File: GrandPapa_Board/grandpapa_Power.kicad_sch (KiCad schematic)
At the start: 34 parts, among them U2 TPS61023DRLT, U5 FPF2124, U6 INA180

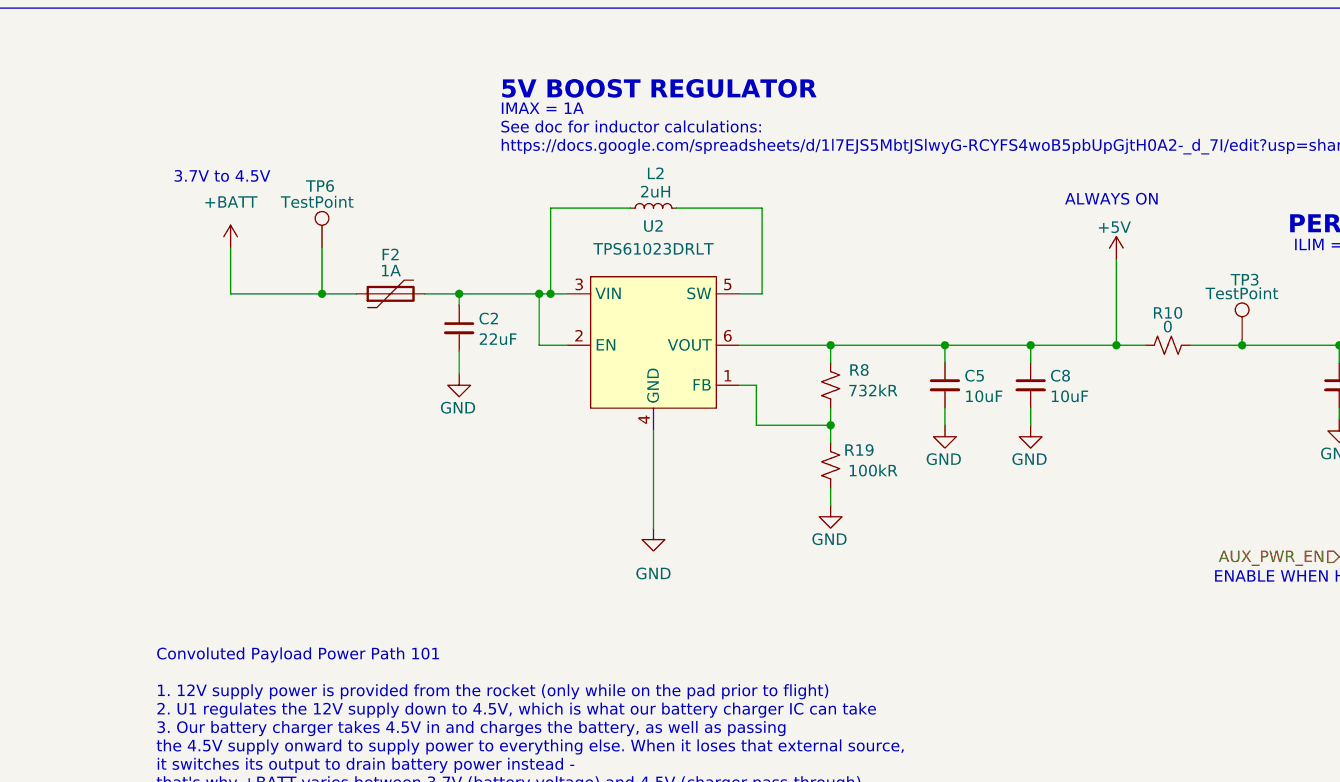
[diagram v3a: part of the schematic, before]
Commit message: Addded 5V boost and kalman board connector
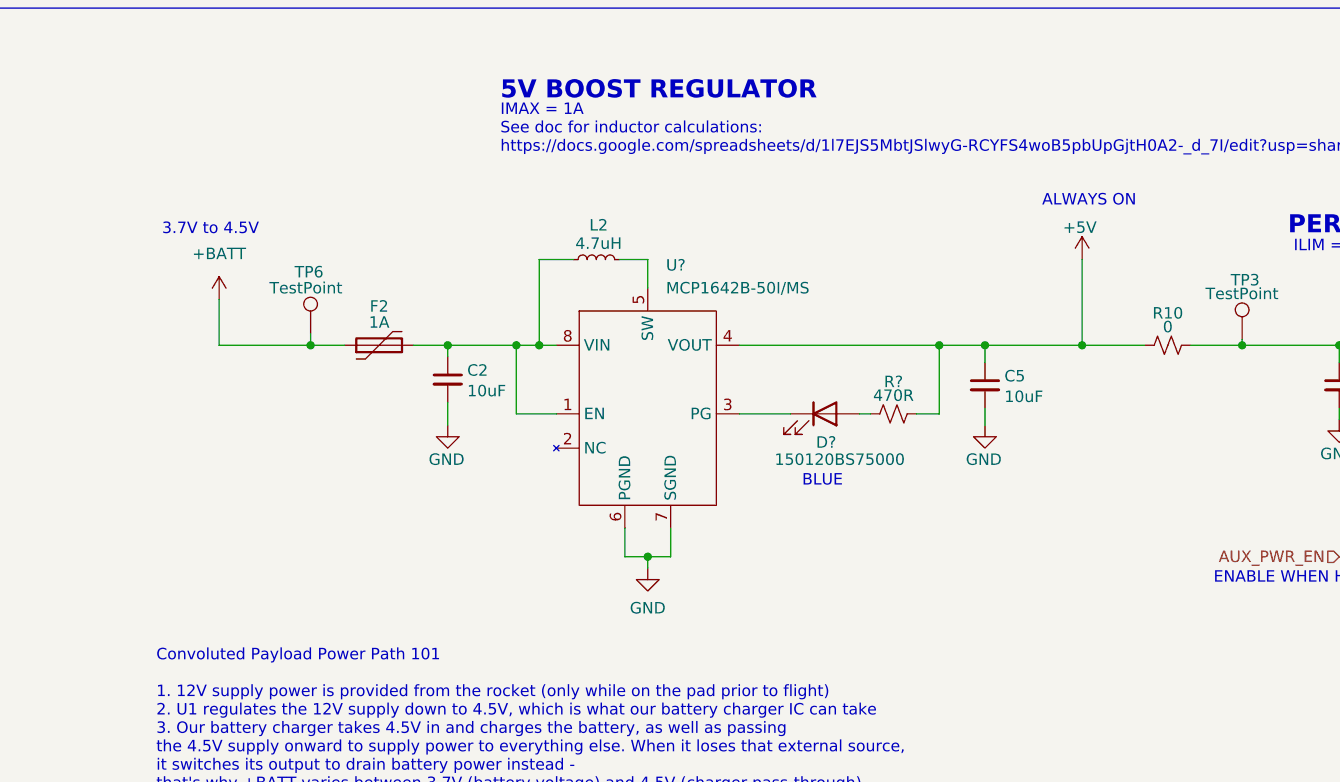
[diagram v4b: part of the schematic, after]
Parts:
- removed C8: 10uF, symbol Device:C_Small
- removed R19: 100kR, symbol Device:R_Small_US
- removed R8: 732kR, symbol Device:R_Small_US
- removed U2: TPS61023DRLT, symbol grandpapa board:TPS61023DRLT
- added D?: 150120BS75000, LED_SMD:LED_1206_3216Metric_Pad1.42x1.75mm_HandSolder, symbol Device:LED
- added R?: 470R, symbol Device:R_Small_US
- added U?: MCP1642B-50I/MS, symbol grandpapa board:MCP1642B/D-xx
- C2: value 22uF -> 10uF
- L2: value 2uH -> 4.7uH
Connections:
- net +5V: now also R?.2, U?.4 (VOUT)
- net GND: now also U?.6 (PGND), U?.7 (SGND)
- net at C2.1, F2.2, L2.1: now also U?.1 (EN), U?.8 (VIN)
- net at L2.2: now also U?.5 (SW)
- new net: D?.1 (K), U?.3 (PG)
- new net: D?.2 (A), R?.1
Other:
- note added: "BLUE"
- moved on the sheet: C2, C5, F2, L2, TP6

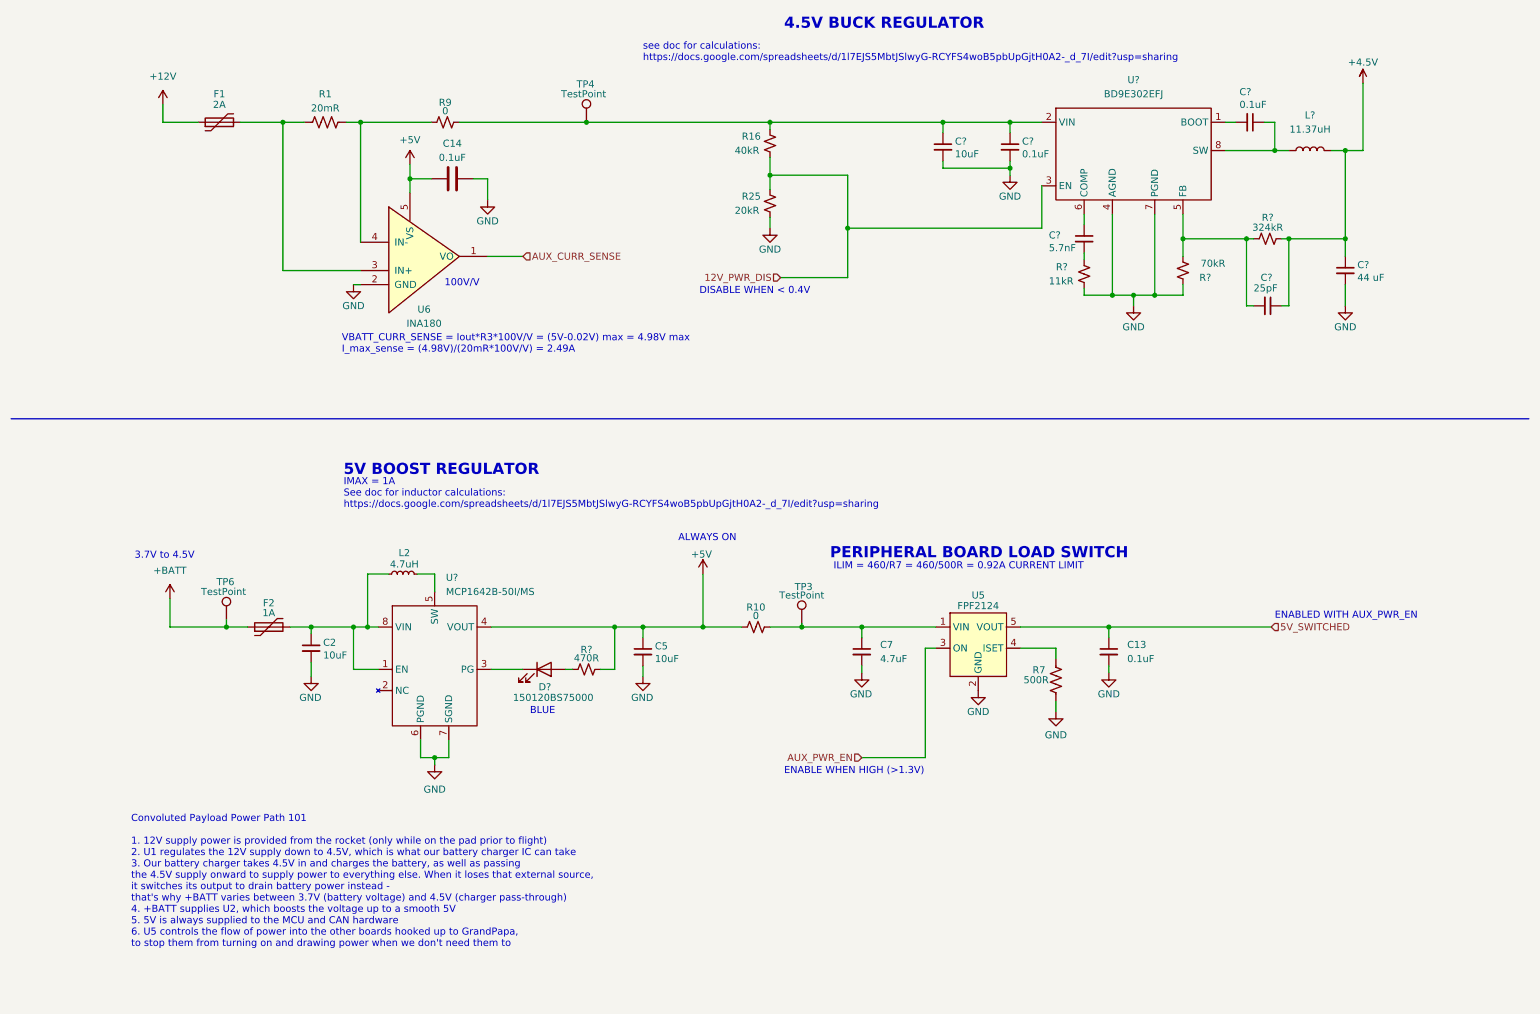
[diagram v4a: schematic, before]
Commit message: minor changes, change some buck converter component values, add inductor + LED part numbers
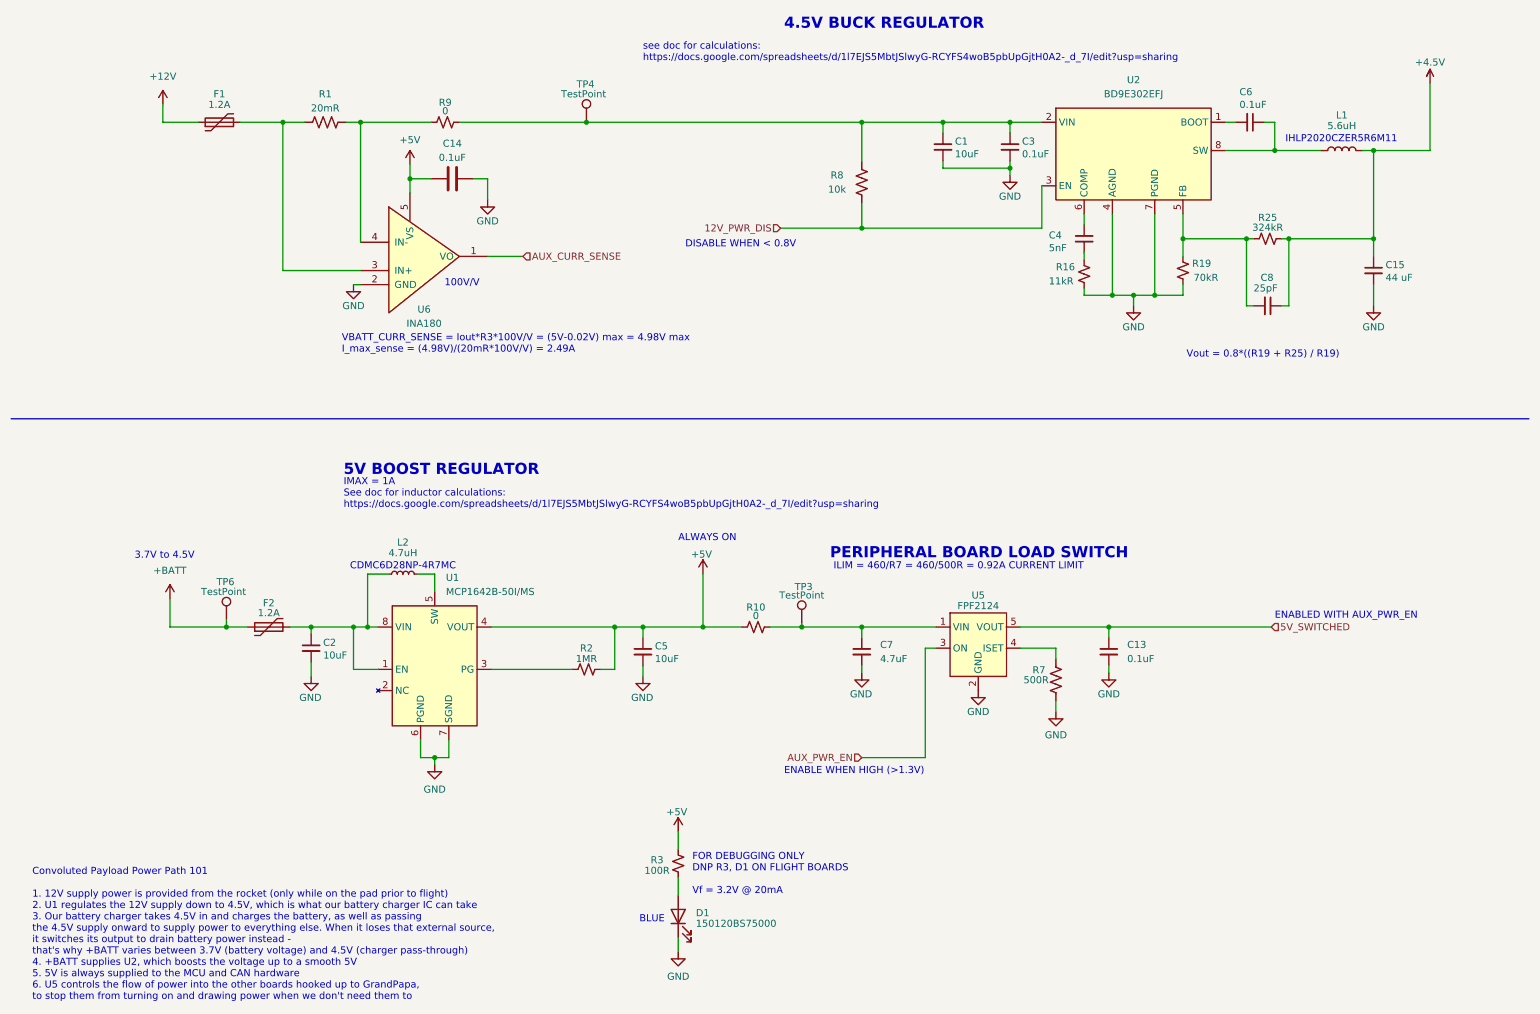
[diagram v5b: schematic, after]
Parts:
- removed R16: 40kR, symbol Device:R_Small_US
- removed R25: 20kR, symbol Device:R_Small_US
- added R2: 1MR, symbol Device:R_Small_US
- added R8: 10k, Resistor_SMD:R_1206_3216Metric_Pad1.30x1.75mm_HandSolder, symbol Device:R_US
- C4: renamed from C?; value 5.7nF -> 5nF
- F1: value 2A -> 1.2A
- F2: value 1A -> 1.2A
- L1: renamed from L?; value 11.37uH -> 5.6uH
- R3: renamed from R?; value 470R -> 100R
- gave numbers to parts that had none: 11
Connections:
- net +5V: now also R2.1
- net 12V_PWR_DIS: now also R8.2
- net GND: now also D1.1 (K)
- net at U1.3 (PG): now also R2.2; no longer D1.1 (K)
- net at C1.1, C3.1, R9.2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: now also R8.1
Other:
- note added: "CDMC6D28NP-4R7MC"
- note added: "DISABLE WHEN < 0.8V"
- note added: "FOR DEBUGGING ONLY DNP R3, D1 ON FLIGHT BOARDS Vf = 3.2V @ 20mA"
- note added: "IHLP2020CZER5R6M11"
- note added: "Vout = 0.8*((R19 + R25) / R19)"
- note removed: "DISABLE WHEN < 0.4V"
- moved on the sheet: C15, D1, L1, R3

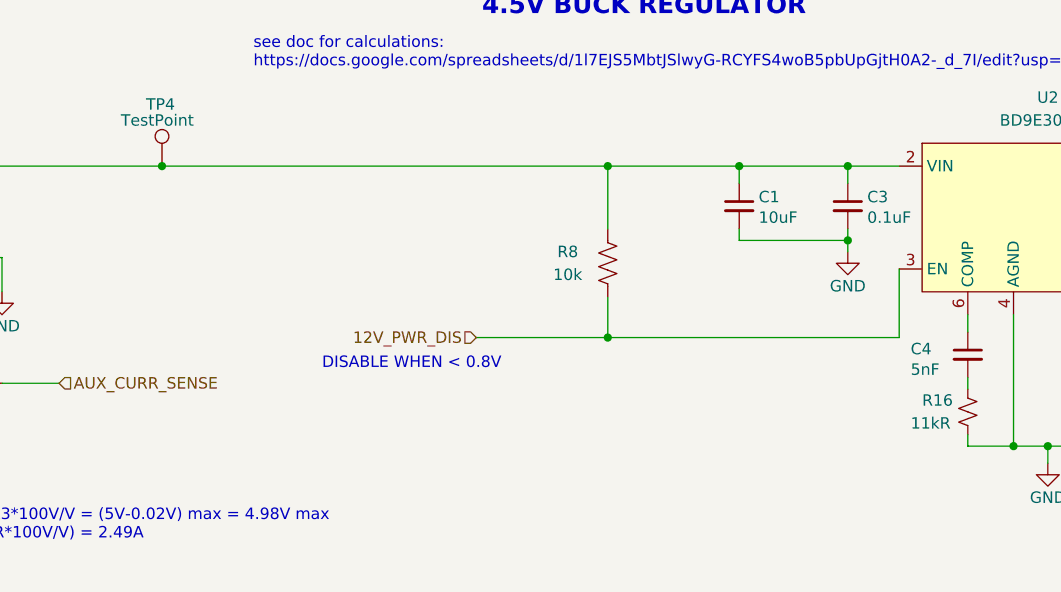
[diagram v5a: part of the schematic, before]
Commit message: fix 4.5V buck reg enable pin
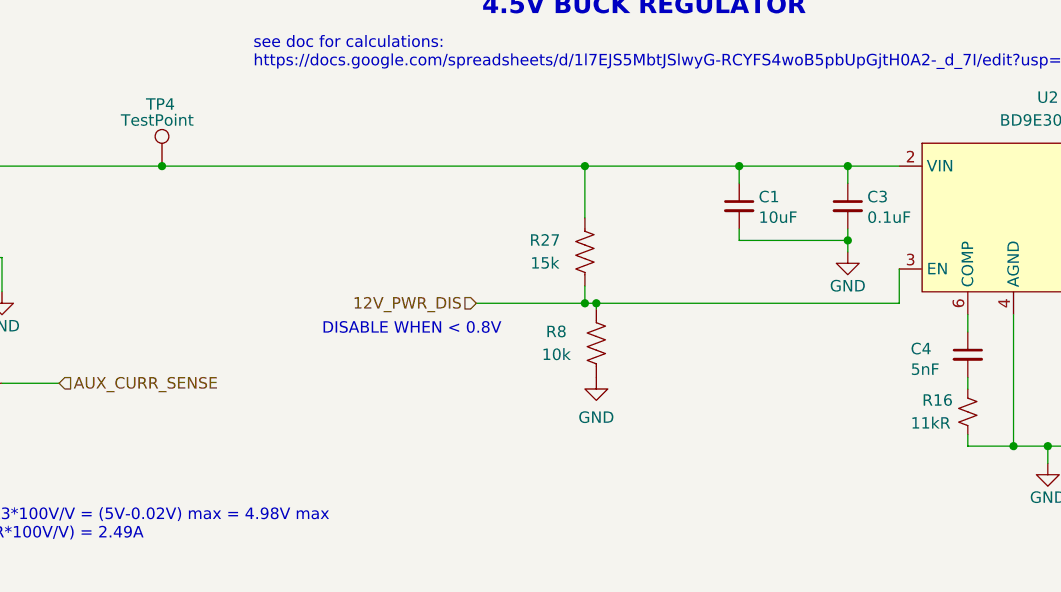
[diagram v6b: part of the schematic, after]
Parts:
- added R27: 15k, Resistor_SMD:R_1206_3216Metric_Pad1.30x1.75mm_HandSolder, symbol Device:R_US
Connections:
- net 12V_PWR_DIS: now also R8.1, R27.2; no longer R8.2
- net GND: now also R8.2
- net at C1.1, C3.1, R9.2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: now also R27.1; no longer R8.1
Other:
- moved on the sheet: R8
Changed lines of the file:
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@@
   (junction (at 234.315 56.515) (diameter 0) (color 0 0 0 0)
   )
-  (junction (at 165.1 54.61) (diameter 0) (color 0 0 0 0)
-  )
   (junction (at 88.265 149.86) (diameter 0) (color 0 0 0 0)
   )
@@
   (junction (at 136.525 126.365) (diameter 0) (color 0 0 0 0)
   )
+  (junction (at 163.83 50.8) (diameter 0) (color 0 0 0 0)
+  )
   (junction (at 222.885 56.515) (diameter 0) (color 0 0 0 0)
   )
@@
   (junction (at 217.805 66.675) (diameter 0) (color 0 0 0 0)
   )
-  (junction (at 165.1 35.56) (diameter 0) (color 0 0 0 0)
-  )
   (junction (at 241.935 56.515) (diameter 0) (color 0 0 0 0)
   )
   (junction (at 60.96 35.56) (diameter 0) (color 0 0 0 0)
   )
+  (junction (at 162.56 35.56) (diameter 0) (color 0 0 0 0)
+  )
   (junction (at 191.77 35.56) (diameter 0) (color 0 0 0 0)
   )
   (junction (at 257.175 40.64) (diameter 0) (color 0 0 0 0)
   )
+  (junction (at 162.56 50.8) (diameter 0) (color 0 0 0 0)
+  )
   (junction (at 125.73 126.365) (diameter 0) (color 0 0 0 0)
   )
@@
   (junction (at 115.57 35.56) (diameter 0) (color 0 0 0 0)
   )
-  (wire (pts (xy 165.1 35.56) (xy 165.1 42.545))
+  (wire (pts (xy 163.83 50.8) (xy 163.83 51.435))
     (stroke (width 0) (type default) (color 0 0 0 0))
   )
@@
     (stroke (width 0) (type default) (color 0 0 0 0))
   )
-  (wire (pts (xy 150.495 54.61) (xy 165.1 54.61))
-    (stroke (width 0) (type default) (color 0 0 0 0))
-  )
   (wire (pts (xy 83.82 43.18) (xy 83.82 45.72))
     (stroke (width 0) (type default) (color 0 0 0 0))
@@
     (stroke (width 0) (type default) (color 0 0 0 0))
   )
-  (wire (pts (xy 197.485 54.61) (xy 197.485 46.99))
-    (stroke (width 0) (type default) (color 0 0 0 0))
-  )
   (wire (pts (xy 210.185 66.675) (xy 213.995 66.675))
     (stroke (width 0) (type default) (color 0 0 0 0))
@@
     (stroke (width 0) (type default) (color 0 0 0 0))
   )
+  (wire (pts (xy 197.485 50.8) (xy 197.485 46.99))
+    (stroke (width 0) (type default) (color 0 0 0 0))
+  )
+  (wire (pts (xy 163.83 50.8) (xy 197.485 50.8))
+    (stroke (width 0) (type default) (color 0 0 0 0))
+  )
   (wire (pts (xy 217.805 52.07) (xy 217.805 66.675))
     (stroke (width 0) (type default) (color 0 0 0 0))
   )
-  (wire (pts (xy 165.1 35.56) (xy 179.705 35.56))
+  (wire (pts (xy 115.57 35.56) (xy 162.56 35.56))
     (stroke (width 0) (type default) (color 0 0 0 0))
   )
@@
     (stroke (width 0) (type default) (color 0 0 0 0))
   )
+  (wire (pts (xy 162.56 35.56) (xy 179.705 35.56))
+    (stroke (width 0) (type default) (color 0 0 0 0))
+  )
   (wire (pts (xy 209.55 134.62) (xy 209.55 133.35))
     (stroke (width 0) (type default) (color 0 0 0 0))
@@
     (stroke (width 0) (type default) (color 0 0 0 0))
   )
+  (wire (pts (xy 162.56 48.895) (xy 162.56 50.8))
+    (stroke (width 0) (type default) (color 0 0 0 0))
+  )
   (wire (pts (xy 88.265 149.86) (xy 90.805 149.86))
     (stroke (width 0) (type default) (color 0 0 0 0))
@@
     (stroke (width 0) (type default) (color 0 0 0 0))
   )
-  (wire (pts (xy 165.1 54.61) (xy 197.485 54.61))
+  (wire (pts (xy 150.495 50.8) (xy 162.56 50.8))
     (stroke (width 0) (type default) (color 0 0 0 0))
   )
@@
     (stroke (width 0) (type default) (color 0 0 0 0))
   )
+  (wire (pts (xy 162.56 35.56) (xy 162.56 41.275))
+    (stroke (width 0) (type default) (color 0 0 0 0))
+  )
   (wire (pts (xy 136.525 126.365) (xy 143.51 126.365))
     (stroke (width 0) (type default) (color 0 0 0 0))
@@
     (stroke (width 0) (type default) (color 0 0 0 0))
   )
+  (wire (pts (xy 162.56 50.8) (xy 163.83 50.8))
+    (stroke (width 0) (type default) (color 0 0 0 0))
+  )
   (wire (pts (xy 176.53 130.175) (xy 178.435 130.175))
     (stroke (width 0) (type default) (color 0 0 0 0))
@@
     (stroke (width 0) (type default) (color 0 0 0 0))
   )
-  (wire (pts (xy 165.1 50.165) (xy 165.1 54.61))
-    (stroke (width 0) (type default) (color 0 0 0 0))
-  )
-  (wire (pts (xy 115.57 35.56) (xy 165.1 35.56))
-    (stroke (width 0) (type default) (color 0 0 0 0))
-  )
   (wire (pts (xy 120.65 133.985) (xy 120.65 126.365))
     (stroke (width 0) (type default) (color 0 0 0 0))
@@
     (effects (font (size 1.27 1.27)) (justify left bottom))
   )
-  (text "DISABLE WHEN < 0.8V\n\n" (at 133.35 60.325 0)
+  (text "DISABLE WHEN < 0.8V\n\n" (at 133.35 56.515 0)
     (effects (font (size 1.27 1.27)) (justify left bottom))
   )
@@
     (effects (font (size 1.27 1.27)) (justify left bottom))
   )
-  (hierarchical_label "12V_PWR_DIS" (shape input) (at 150.495 54.61 180)
+  (hierarchical_label "12V_PWR_DIS" (shape input) (at 150.495 50.8 180)
     (effects (font (size 1.27 1.27)) (justify right))
   )
@@
     )
     (pin "1")
+  )
+  (symbol (lib_id "Device:R_US") (at 162.56 45.085 0) (unit 1)
+    (in_bom yes) (on_board yes)
+    (property "Reference" "R27" (id 0) (at 158.115 43.815 0))
+    (property "Value" "15k" (id 1) (at 158.115 46.355 0))
+    (property "Footprint" "Resistor_SMD:R_1206_3216Metric_Pad1.30x1.75mm_HandSolder" (id 2) (at 163.576 45.339 90)
+      (effects (font (size 1.27 1.27)) hide)
+    )
+    (property "Datasheet" "~" (id 3) (at 162.56 45.085 0)
+      (effects (font (size 1.27 1.27)) hide)
+    )
+    (pin "1")
+    (pin "2")
   )
   (symbol (lib_id "power:GND") (at 88.265 151.13 0) (unit 1)
@@
     (pin "2")
   )
-  (symbol (lib_id "Device:R_US") (at 165.1 46.355 0) (unit 1)
-    (in_bom yes) (on_board yes)
-    (property "Reference" "R8" (id 0) (at 160.655 45.085 0))
-    (property "Value" "10k" (id 1) (at 160.655 47.625 0))
-    (property "Footprint" "Resistor_SMD:R_1206_3216Metric_Pad1.30x1.75mm_HandSolder" (id 2) (at 166.116 46.609 90)
-      (effects (font (size 1.27 1.27)) hide)
-    )
-    (property "Datasheet" "~" (id 3) (at 165.1 46.355 0)
+  (symbol (lib_id "Device:R_US") (at 163.83 55.245 0) (unit 1)
+    (in_bom yes) (on_board yes)
+    (property "Reference" "R8" (id 0) (at 159.385 53.975 0))
+    (property "Value" "10k" (id 1) (at 159.385 56.515 0))
+    (property "Footprint" "Resistor_SMD:R_1206_3216Metric_Pad1.30x1.75mm_HandSolder" (id 2) (at 164.846 55.499 90)
+      (effects (font (size 1.27 1.27)) hide)
+    )
+    (property "Datasheet" "~" (id 3) (at 163.83 55.245 0)
       (effects (font (size 1.27 1.27)) hide)
     )
@@
     (pin "2")
   )
+  (symbol (lib_id "power:GND") (at 163.83 59.055 0) (unit 1)
+    (in_bom yes) (on_board yes) (fields_autoplaced)
+    (property "Reference" "#PWR057" (id 0) (at 163.83 65.405 0)
+      (effects (font (size 1.27 1.27)) hide)
+    )
+    (property "Value" "GND" (id 1) (at 163.83 63.5 0))
+    (property "Footprint" "" (id 2) (at 163.83 59.055 0)
+      (effects (font (size 1.27 1.27)) hide)
+    )
+    (property "Datasheet" "" (id 3) (at 163.83 59.055 0)
+      (effects (font (size 1.27 1.27)) hide)
+    )
+    (pin "1")
+  )
   (symbol (lib_id "power:GND") (at 97.79 49.53 0) (unit 1)
